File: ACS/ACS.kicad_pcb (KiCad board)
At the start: 2 copper layers, 50 x 140 mm, 7 parts, among them J1 Screw_Terminal_01x02, Q1 IRLB8721PBF, Q2 IRLB8721PBF

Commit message: Add footprint for WT901
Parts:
- added REF**: WT901, IMU:WT901, F.Cu at (70.0, 39.0)
- moved J1 18.5 mm to (109.2, 153.5), turned to -90 degrees

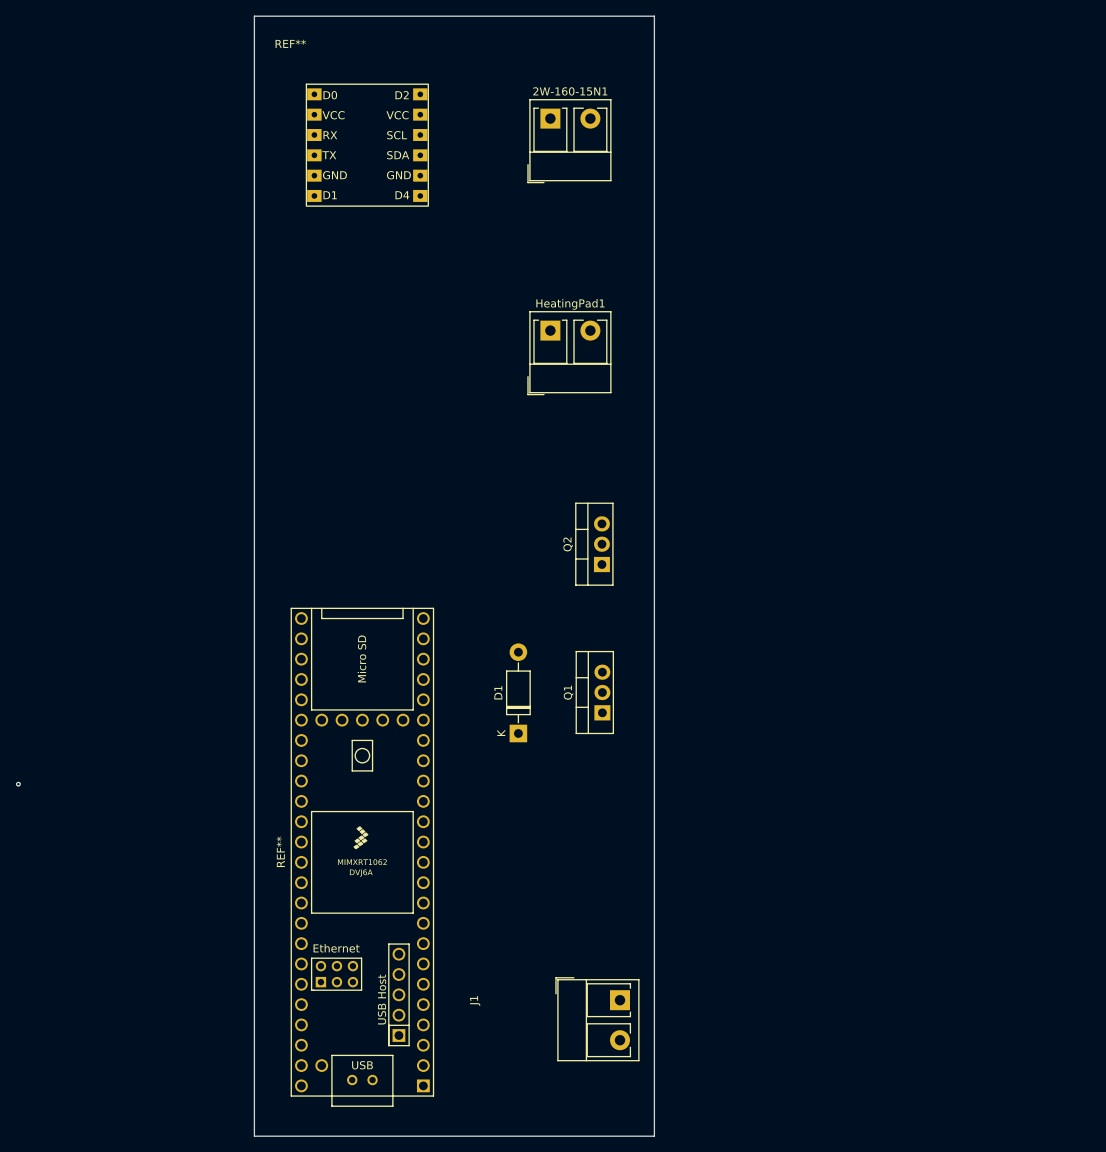
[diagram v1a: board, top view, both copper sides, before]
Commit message: fixed error for U2
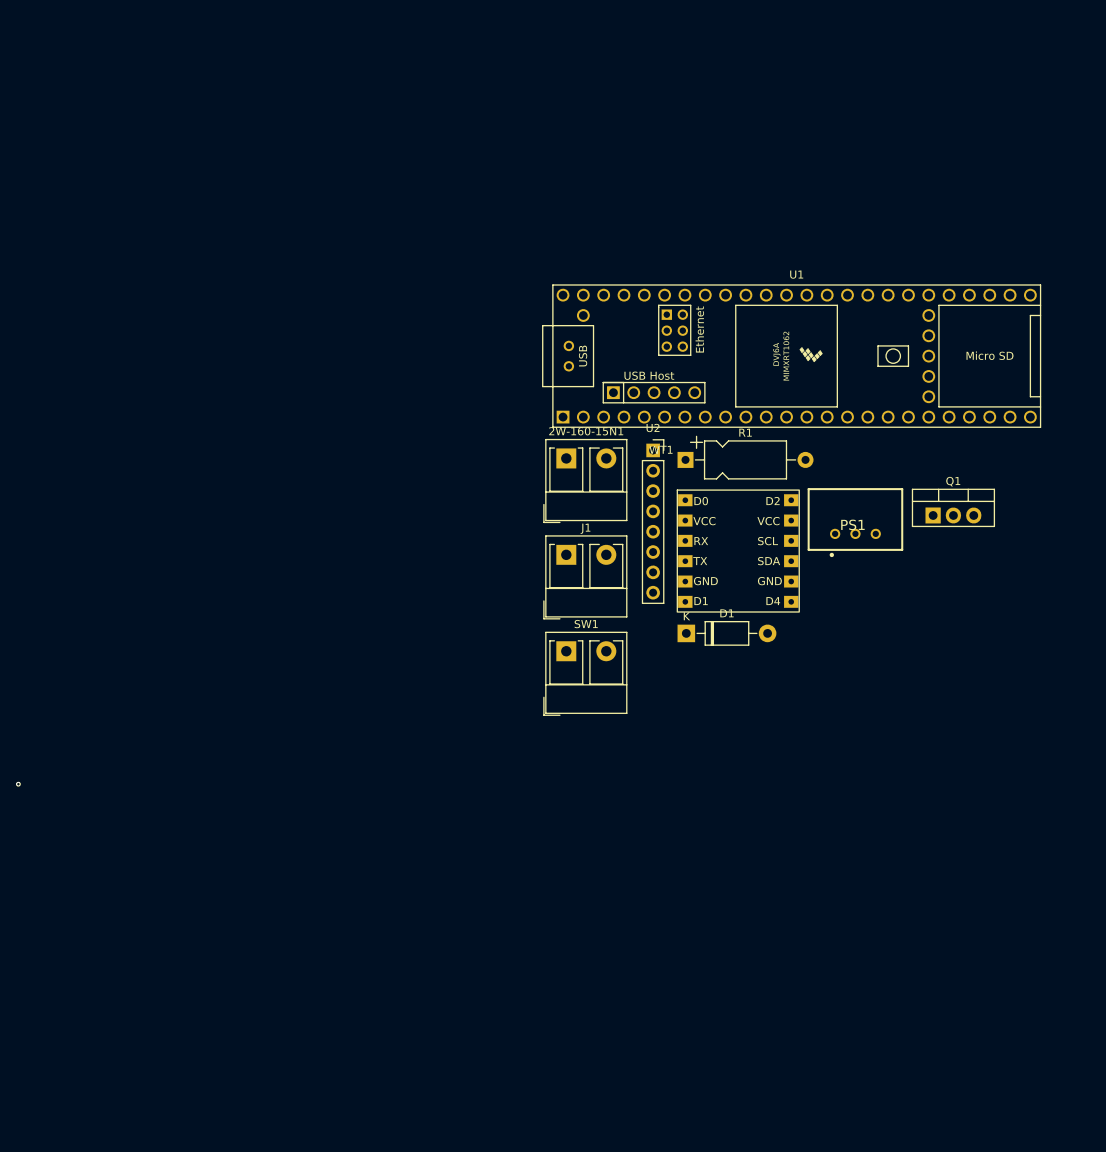
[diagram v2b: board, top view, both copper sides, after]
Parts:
- removed HeatingPad1: ~, TerminalBlock_RND:TerminalBlock_RND_205-00276_1x02_P5.00mm_Vertical
- removed Q2: IRLB8721PBF, Package_TO_SOT_THT:TO-220-3_Vertical
- removed REF**: WT901, IMU:WT901
- removed REF**: Teensy 4.1, Teensy41
- added PS1: TSR_1-2450, random-footprints:TSR-1-24120, F.Cu at (138.6, 95.2)
- added R1: 270, Capacitor_THT:CP_Axial_L10.0mm_D4.5mm_P15.00mm_Horizontal, F.Cu at (117.4, 86.0)
- added SW1: SW_SPDT, TerminalBlock_RND:TerminalBlock_RND_205-00276_1x02_P5.00mm_Vertical, F.Cu at (102.5, 109.9)
- added U1: Teensy4.1, teensy-foots:Teensy41, F.Cu at (131.3, 73.0)
- added U2: ~, Connector_PinSocket_2.54mm:PinSocket_1x08_P2.54mm_Vertical, F.Cu at (113.3, 84.8)
- added WT1: ~, Library:WT901, F.Cu at (116.4, 89.7)
- moved J1 56.1 mm to (102.5, 97.8), turned to 0 degrees
- moved Q1 48.1 mm to (148.3, 92.9), turned to 0 degrees
- moved 2W-160-15N1 42.5 mm to (102.5, 85.8)
- moved D1 24.4 mm to (117.5, 107.7), turned to 0 degrees
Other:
- board outline removed

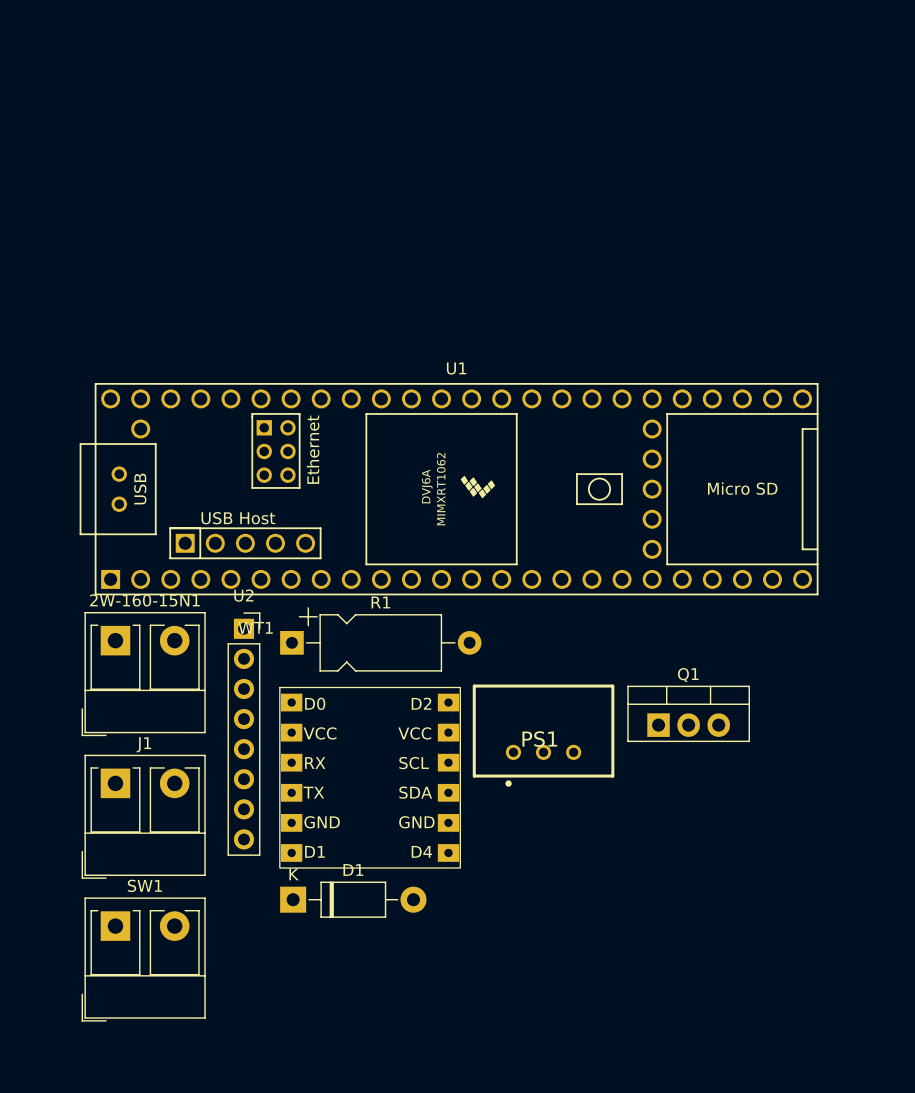
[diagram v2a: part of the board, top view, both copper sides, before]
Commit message: finished traces for acs and generated gerber files
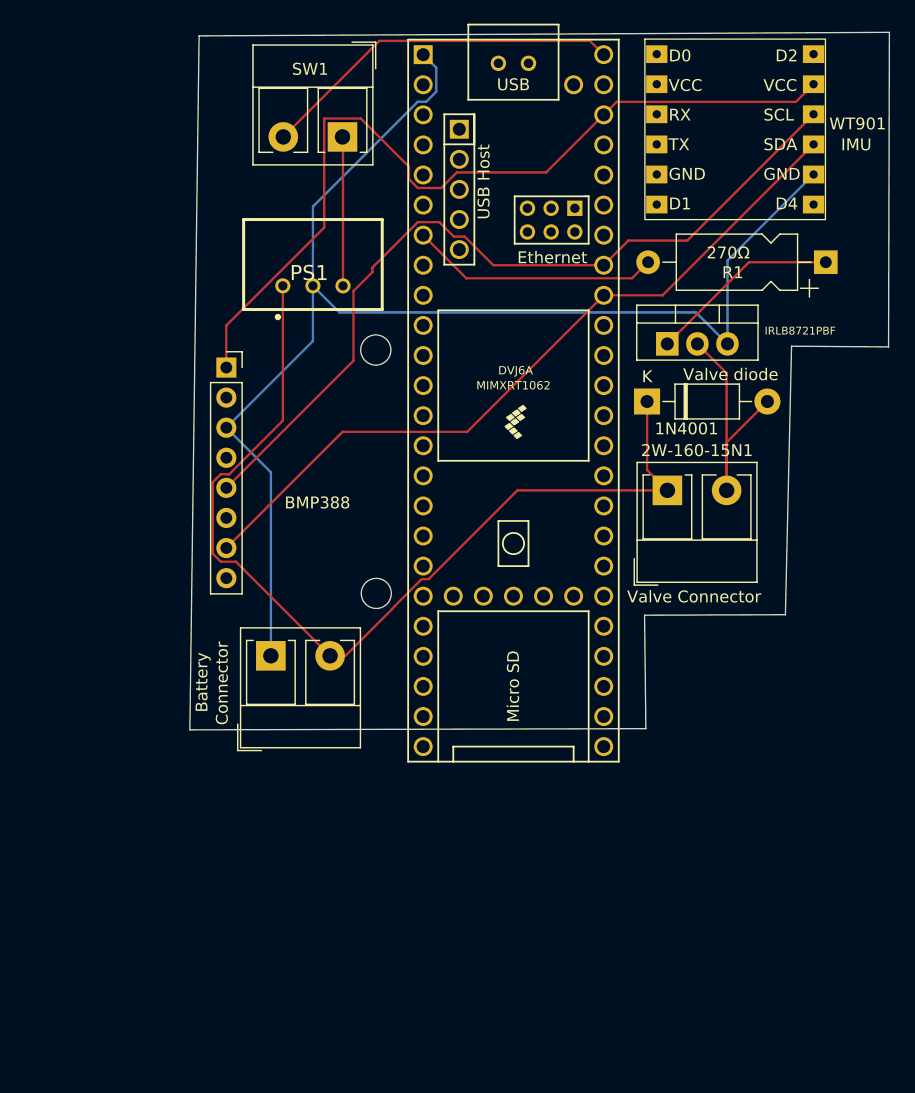
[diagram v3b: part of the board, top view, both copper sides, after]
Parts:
- removed D1: 1N4001, Diode_THT:D_DO-41_SOD81_P10.16mm_Horizontal
- removed J1: Screw_Terminal_01x02, TerminalBlock_RND:TerminalBlock_RND_205-00276_1x02_P5.00mm_Vertical
- removed Q1: IRLB8721PBF, Package_TO_SOT_THT:TO-220-3_Vertical
- removed U2: ~, Connector_PinSocket_2.54mm:PinSocket_1x08_P2.54mm_Vertical
- removed WT1: ~, Library:WT901
- added BMP388: ~, Connector_PinSocket_2.54mm:PinSocket_1x08_P2.54mm_Vertical, F.Cu at (111.8, 62.7)
- added Battery: Battery Screw_Terminal_01x02, TerminalBlock_RND:TerminalBlock_RND_205-00276_1x02_P5.00mm_Vertical, F.Cu at (115.6, 87.1)
- added IRLB8721PBF: IRLB8721PBF, Package_TO_SOT_THT:TO-220-3_Vertical, F.Cu at (149.1, 60.7)
- added Valve diode: 1N4001, Diode_THT:D_DO-41_SOD81_P10.16mm_Horizontal, F.Cu at (147.4, 65.6)
- added WT901: ~, Library:WT901, F.Cu at (147.2, 35.0)
- SW1: value SW_SPDT -> SW_DPST_x2
- moved SW1 69.3 mm to (121.7, 43.2), turned to 180 degrees
- moved R1 55.4 mm to (162.5, 53.8), turned to 180 degrees
- moved 2W-160-15N1 48.3 mm to (149.1, 73.1)
- moved PS1 43.9 mm to (119.2, 55.8)
- moved U1 8.88 mm to (136.1, 65.5), turned to -90 degrees
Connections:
- SW1 pad 1: unconnected-(SW1-A-Pad1) -> Net-(PS1-VOUT+)
- SW1 pad 2: Net-(PS1-VOUT+) -> /5VIN
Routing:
- net GND: track 0.00 -> 114.9 mm
- net +12V: track 0.00 -> 103.8 mm
- net +3V3: track 0.00 -> 72.4 mm
- net /SCL: track 0.00 -> 69.4 mm
- net /SDA: track 0.00 -> 63.7 mm
- net /5VIN: track 0.00 -> 30.9 mm
- net /Valve Signal: track 0.00 -> 21.1 mm
- net Net-(Q1-G): track 0.00 -> 16.2 mm
- net Net-(PS1-VOUT+): track 0.00 -> 12.6 mm
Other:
- board outline added: 59.1 x 58.9 mm
- board text added: "1N4001"
- board text added: "270Ω"
- board text added: "Connector"
- board text added: "IMU"
- board text added: "Valve Connector"
